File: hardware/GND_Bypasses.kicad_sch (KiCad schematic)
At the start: 12 parts, among them Q1 NPN

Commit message: updated sheets and 1st review changes
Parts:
- removed C131: 0.1uF, symbol Device:C_Small
- removed C132: 0.22uF, symbol Device:C_Small
- removed Q1: NPN, symbol Simulation_SPICE:NPN
- removed R97: 100, symbol Device:R_Small
- removed R98: 200, symbol Device:R_Small
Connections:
- net GNDA renamed AVSS
- net GNDC renamed CVSS
- net GNDD renamed DVSS
- net GNDR renamed REFHM
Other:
- moved on the sheet: C122, C123, C128, C129, C130, C133, C134

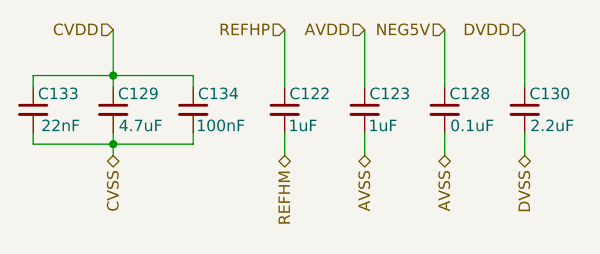
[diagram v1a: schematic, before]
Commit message: updated sheets, footprint, and calcs; 2nd review changes
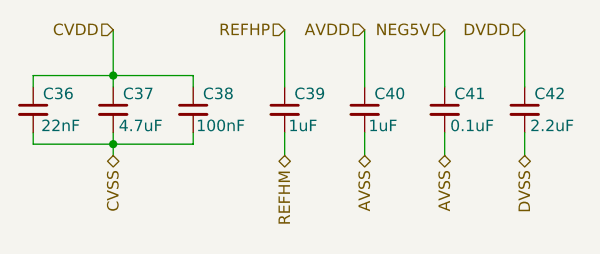
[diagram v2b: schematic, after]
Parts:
- renumbered C133 to C36, C129 to C37, C134 to C38, C122 to C39, C123 to C40, C128 to C41, C130 to C42
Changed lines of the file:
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@@
 		(in_pos_files yes)
 		(dnp no)
-		(property "Reference" "C122"
+		(property "Reference" "C39"
 			(at 142.494 92.202 0)
 			(show_name no)
@@
 			(project "PS-SegmentMonitoringBoard"
 				(path "/f5c3f134-fd91-4d3b-aae6-719b554b2d69/d887bdd7-4ddc-43ee-a27d-51208f676d2d"
-					(reference "C122")
+					(reference "C39")
 					(unit 1)
 				)
@@
 		(in_pos_files yes)
 		(dnp no)
-		(property "Reference" "C123"
+		(property "Reference" "C40"
 			(at 151.384 92.202 0)
 			(show_name no)
@@
 			(project "PS-SegmentMonitoringBoard"
 				(path "/f5c3f134-fd91-4d3b-aae6-719b554b2d69/d887bdd7-4ddc-43ee-a27d-51208f676d2d"
-					(reference "C123")
+					(reference "C40")
 					(unit 1)
 				)
@@
 		(in_pos_files yes)
 		(dnp no)
-		(property "Reference" "C133"
+		(property "Reference" "C36"
 			(at 114.554 92.202 0)
 			(show_name no)
@@
 			(project "PS-SegmentMonitoringBoard"
 				(path "/f5c3f134-fd91-4d3b-aae6-719b554b2d69/d887bdd7-4ddc-43ee-a27d-51208f676d2d"
-					(reference "C133")
+					(reference "C36")
 					(unit 1)
 				)
@@
 		(in_pos_files yes)
 		(dnp no)
-		(property "Reference" "C134"
+		(property "Reference" "C38"
 			(at 132.334 92.202 0)
 			(show_name no)
@@
 			(project "PS-SegmentMonitoringBoard"
 				(path "/f5c3f134-fd91-4d3b-aae6-719b554b2d69/d887bdd7-4ddc-43ee-a27d-51208f676d2d"
-					(reference "C134")
+					(reference "C38")
 					(unit 1)
 				)
@@
 		(in_pos_files yes)
 		(dnp no)
-		(property "Reference" "C128"
+		(property "Reference" "C41"
 			(at 160.274 92.202 0)
 			(show_name no)
@@
 			(project "PS-SegmentMonitoringBoard"
 				(path "/f5c3f134-fd91-4d3b-aae6-719b554b2d69/d887bdd7-4ddc-43ee-a27d-51208f676d2d"
-					(reference "C128")
+					(reference "C41")
 					(unit 1)
 				)
@@
 		(in_pos_files yes)
 		(dnp no)
-		(property "Reference" "C129"
+		(property "Reference" "C37"
 			(at 123.444 92.202 0)
 			(show_name no)
@@
 			(project "PS-SegmentMonitoringBoard"
 				(path "/f5c3f134-fd91-4d3b-aae6-719b554b2d69/d887bdd7-4ddc-43ee-a27d-51208f676d2d"
-					(reference "C129")
+					(reference "C37")
 					(unit 1)
 				)
@@
 		(in_pos_files yes)
 		(dnp no)
-		(property "Reference" "C130"
+		(property "Reference" "C42"
 			(at 169.164 92.202 0)
 			(show_name no)
@@
 			(project "PS-SegmentMonitoringBoard"
 				(path "/f5c3f134-fd91-4d3b-aae6-719b554b2d69/d887bdd7-4ddc-43ee-a27d-51208f676d2d"
-					(reference "C130")
-					(unit 1)
-				)
+					(reference "C42")
+					(unit 1)
+				)
